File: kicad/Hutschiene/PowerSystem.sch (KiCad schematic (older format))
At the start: 16 parts, among them P201 Mode_Bridge, U201 LF120ABDT-TR, U202 TPS70933

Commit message: Further work on the redesign
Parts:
- removed D201: 12VDC, LEDs:LED_0805, symbol LED
- removed R203: 2k4Ω, Resistors_SMD:R_0805, symbol R
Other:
- moved on the sheet: TP202
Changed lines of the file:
@@
 U+
 $Comp
-L GND #PWR016
+L GND #PWR017
 U 1 1 584DB061
 P 3900 4850
-F 0 "#PWR016" H 3900 4600 50  0001 C CNN
+F 0 "#PWR017" H 3900 4600 50  0001 C CNN
 F 1 "GND" H 3900 4700 50  0000 C CNN
 F 2 "" H 3900 4850 50  0000 C CNN
@@
 $EndComp
 $Comp
-L GND #PWR017
+L GND #PWR018
 U 1 1 584DB084
 P 5250 5300
-F 0 "#PWR017" H 5250 5050 50  0001 C CNN
+F 0 "#PWR018" H 5250 5050 50  0001 C CNN
 F 1 "GND" H 5250 5150 50  0000 C CNN
 F 2 "" H 5250 5300 50  0000 C CNN
@@
 UbOut
 Wire Wire Line
-	4450 1400 6150 1400
+	4450 1400 5550 1400
 Wire Wire Line
 	2800 1400 3350 1400
@@
 $EndComp
 $Comp
-L GND #PWR018
+L GND #PWR019
 U 1 1 584DD17A
 P 3900 2650
-F 0 "#PWR018" H 3900 2400 50  0001 C CNN
+F 0 "#PWR019" H 3900 2400 50  0001 C CNN
 F 1 "GND" H 3900 2500 50  0000 C CNN
 F 2 "" H 3900 2650 50  0000 C CNN
@@
 	1    0    0    -1
 $EndComp
-Text HLabel 6150 1400 2    60   Input ~ 0
+Text HLabel 5550 1400 2    60   Input ~ 0
 U+Out
 Text HLabel 2800 1400 0    60   Input ~ 0
@@
 	4600 1700 4600 1400
 Connection ~ 4600 1400
-$Comp
-L LED D201
-U 1 1 584DD7AB
-P 5250 2300
-F 0 "D201" H 5250 2400 50  0000 C CNN
-F 1 "12VDC" H 5250 2200 50  0000 C CNN
-F 2 "LEDs:LED_0805" H 5250 2300 50  0001 C CNN
-F 3 "" H 5250 2300 50  0000 C CNN
-	1    5250 2300
-	0    -1   -1   0
-$EndComp
-Wire Wire Line
-	5250 1400 5250 1650
-Connection ~ 5250 1400
-$Comp
-L R R203
-U 1 1 584DD8C0
-P 5250 1800
-F 0 "R203" V 5330 1800 50  0000 C CNN
-F 1 "2k4Ω" V 5250 1800 50  0000 C CNN
-F 2 "Resistors_SMD:R_0805" V 5180 1800 50  0001 C CNN
-F 3 "" H 5250 1800 50  0000 C CNN
-	1    5250 1800
-	1    0    0    -1
-$EndComp
-$Comp
-L GND #PWR019
-U 1 1 584DD971
-P 5250 2650
-F 0 "#PWR019" H 5250 2400 50  0001 C CNN
-F 1 "GND" H 5250 2500 50  0000 C CNN
-F 2 "" H 5250 2650 50  0000 C CNN
-F 3 "" H 5250 2650 50  0000 C CNN
-	1    5250 2650
-	1    0    0    -1
-$EndComp
-Wire Wire Line
-	5250 2500 5250 2650
-Wire Wire Line
-	5600 1200 5600 1400
-Connection ~ 5600 1400
-Text Label 6000 1400 0    60   ~ 0
+Wire Wire Line
+	5000 1200 5000 1400
+Connection ~ 5000 1400
+Text Label 5400 1400 0    60   ~ 0
 U+
 $Comp
 L TEST_1P TP202
 U 1 1 584E1FA9
-P 5600 1200
-F 0 "TP202" H 5600 1470 50  0000 C CNN
-F 1 "TP12V" H 5600 1400 50  0000 C CNN
-F 2 "Pin_Headers:Pin_Header_Straight_1x01" H 5800 1200 50  0001 C CNN
-F 3 "" H 5800 1200 50  0000 C CNN
-F 4 "Value" H 5600 1200 60  0001 C CNN "MFP"
-F 5 "Value" H 5600 1200 60  0001 C CNN "Conrad-PN"
-F 6 "Value" H 5600 1200 60  0001 C CNN "Digikey-PN"
-	1    5600 1200
+P 5000 1200
+F 0 "TP202" H 5000 1470 50  0000 C CNN
+F 1 "TP12V" H 5000 1400 50  0000 C CNN
+F 2 "Pin_Headers:Pin_Header_Straight_1x01" H 5200 1200 50  0001 C CNN
+F 3 "" H 5200 1200 50  0000 C CNN
+F 4 "Value" H 5000 1200 60  0001 C CNN "MFP"
+F 5 "Value" H 5000 1200 60  0001 C CNN "Conrad-PN"
+F 6 "Value" H 5000 1200 60  0001 C CNN "Digikey-PN"
+	1    5000 1200
 	1    0    0    -1
 $EndComp
@@
 $EndComp
 Wire Wire Line
-	5250 2100 5250 1950
-Wire Wire Line
 	5250 4550 5250 4700

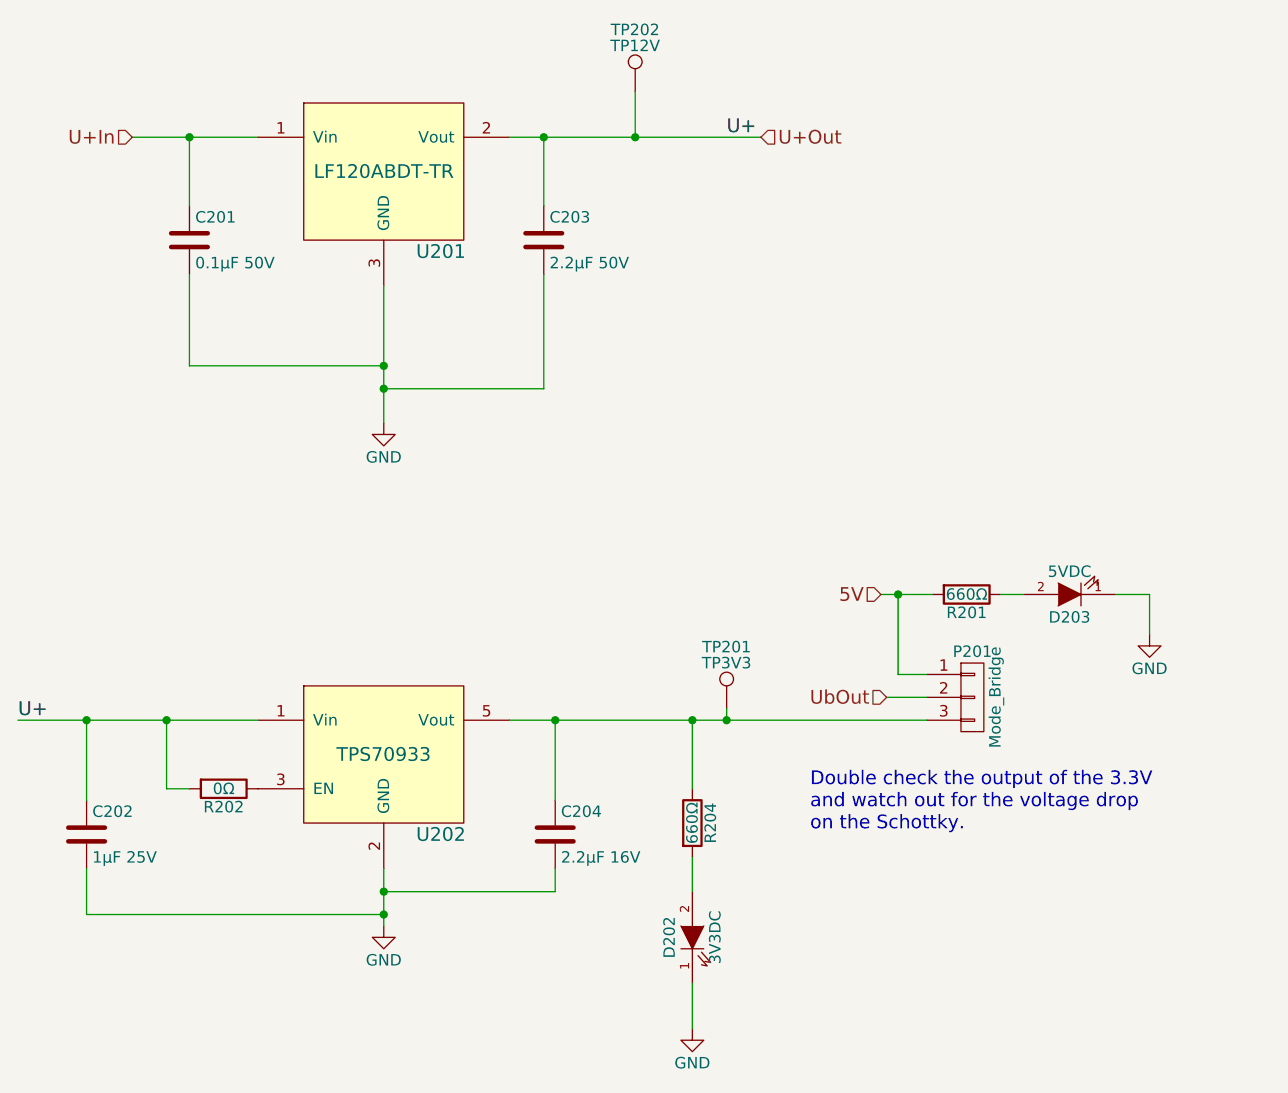
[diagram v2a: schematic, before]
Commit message: Further work on the new Hutschiene Layout
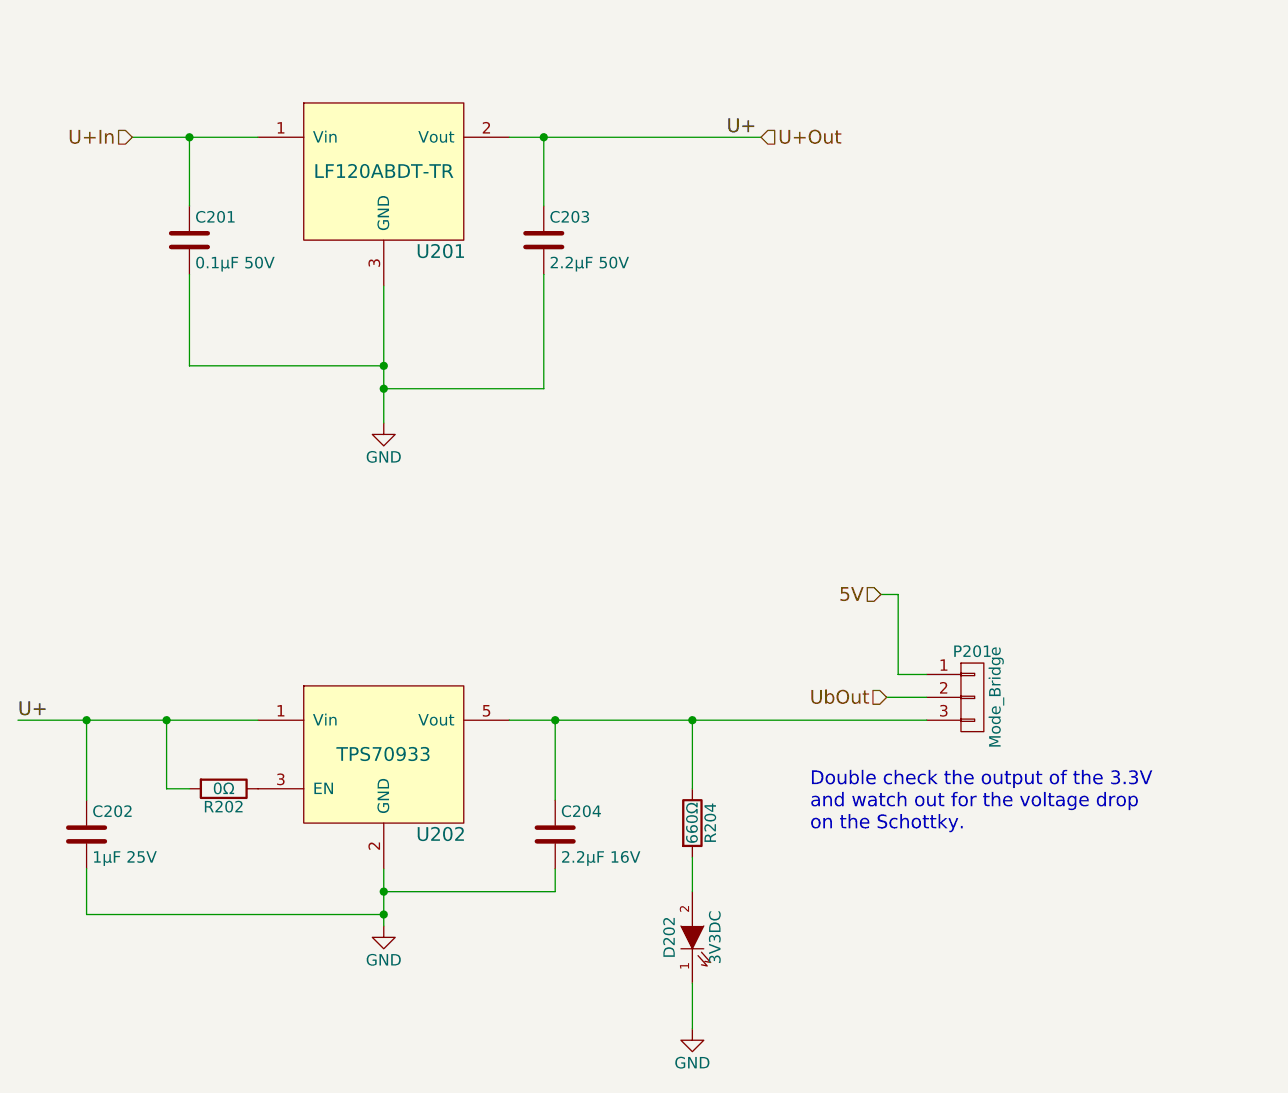
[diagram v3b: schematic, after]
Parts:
- removed D203: 5VDC, LEDs:LED_0805, symbol LED
- removed R201: 660Ω, Resistors_SMD:R_0805, symbol R
- removed TP201: TP3V3, Measurement_Points:Measurement_Point_Round-SMD-Pad_Small, symbol TEST_1P
- removed TP202: TP12V, Pin_Headers:Pin_Header_Straight_1x01, symbol TEST_1P
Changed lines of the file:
@@
 Wire Wire Line
 	5250 5100 5250 5300
-Wire Wire Line
-	5400 3950 5400 3900
-Connection ~ 5400 3950
 Text HLabel 6100 3850 0    60   Input ~ 0
 UbOut
@@
 	4600 1700 4600 1400
 Connection ~ 4600 1400
-Wire Wire Line
-	5000 1200 5000 1400
-Connection ~ 5000 1400
 Text Label 5400 1400 0    60   ~ 0
 U+
-$Comp
-L TEST_1P TP202
-U 1 1 584E1FA9
-P 5000 1200
-F 0 "TP202" H 5000 1470 50  0000 C CNN
-F 1 "TP12V" H 5000 1400 50  0000 C CNN
-F 2 "Pin_Headers:Pin_Header_Straight_1x01" H 5200 1200 50  0001 C CNN
-F 3 "" H 5200 1200 50  0000 C CNN
-F 4 "Value" H 5000 1200 60  0001 C CNN "MFP"
-F 5 "Value" H 5000 1200 60  0001 C CNN "Conrad-PN"
-F 6 "Value" H 5000 1200 60  0001 C CNN "Digikey-PN"
-	1    5000 1200
-	1    0    0    -1
-$EndComp
-$Comp
-L TEST_1P TP201
-U 1 1 584E2106
-P 5400 3900
-F 0 "TP201" H 5400 4170 50  0000 C CNN
-F 1 "TP3V3" H 5400 4100 50  0000 C CNN
-F 2 "Measurement_Points:Measurement_Point_Round-SMD-Pad_Small" H 5600 3900 50  0001 C CNN
-F 3 "" H 5600 3900 50  0000 C CNN
-	1    5400 3900
-	1    0    0    -1
-$EndComp
 Wire Wire Line
 	5250 4550 5250 4700
@@
 Wire Wire Line
 	4450 3950 6275 3950
-$Comp
-L LED D203
-U 1 1 58DCC141
-P 6900 3400
-F 0 "D203" H 6900 3500 50  0000 C CNN
-F 1 "5VDC" H 6900 3300 50  0000 C CNN
-F 2 "LEDs:LED_0805" H 6900 3400 50  0001 C CNN
-F 3 "" H 6900 3400 50  0000 C CNN
-	1    6900 3400
-	-1   0    0    1
-$EndComp
-$Comp
-L GND #PWR020
-U 1 1 58DCC147
-P 7250 3575
-F 0 "#PWR020" H 7250 3325 50  0001 C CNN
-F 1 "GND" H 7250 3425 50  0000 C CNN
-F 2 "" H 7250 3575 50  0000 C CNN
-F 3 "" H 7250 3575 50  0000 C CNN
-	1    7250 3575
-	1    0    0    -1
-$EndComp
-$Comp
-L R R201
-U 1 1 58DCC526
-P 6450 3400
-F 0 "R201" V 6530 3400 50  0000 C CNN
-F 1 "660Ω" V 6450 3400 50  0000 C CNN
-F 2 "Resistors_SMD:R_0805" V 6380 3400 50  0001 C CNN
-F 3 "" H 6450 3400 50  0000 C CNN
-	1    6450 3400
-	0    1    1    0
-$EndComp
 Wire Wire Line
-	6075 3400 6300 3400
-Wire Wire Line
-	6600 3400 6700 3400
-Wire Wire Line
-	7100 3400 7250 3400
-Wire Wire Line
-	7250 3400 7250 3575
+	6075 3400 6150 3400
 Wire Wire Line
 	6275 3750 6150 3750
 Wire Wire Line
 	6150 3750 6150 3400
-Connection ~ 6150 3400
 $EndSCHEMATC

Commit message: Correction to the board connected and seperated out the pwr
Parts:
- C204: footprint Capacitors_SMD:C_1210 -> Capacitors_SMD:C_1206
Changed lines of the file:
@@
 U+
 $Comp
-L GND #PWR017
+L GND #PWR019
 U 1 1 584DB061
 P 3900 4850
-F 0 "#PWR017" H 3900 4600 50  0001 C CNN
+F 0 "#PWR019" H 3900 4600 50  0001 C CNN
 F 1 "GND" H 3900 4700 50  0000 C CNN
 F 2 "" H 3900 4850 50  0000 C CNN
@@
 F 0 "C204" H 4675 4550 50  0000 L CNN
 F 1 "2.2μF 16V" H 4675 4350 50  0000 L CNN
-F 2 "Capacitors_SMD:C_1210" H 4688 4300 50  0001 C CNN
+F 2 "Capacitors_SMD:C_1206" H 4688 4300 50  0001 C CNN
 F 3 "" H 4650 4450 50  0000 C CNN
 F 4 "Value" H 4650 4450 60  0001 C CNN "MFP"
@@
 $EndComp
 $Comp
-L GND #PWR018
+L GND #PWR020
 U 1 1 584DB084
 P 5250 5300
-F 0 "#PWR018" H 5250 5050 50  0001 C CNN
+F 0 "#PWR020" H 5250 5050 50  0001 C CNN
 F 1 "GND" H 5250 5150 50  0000 C CNN
 F 2 "" H 5250 5300 50  0000 C CNN
@@
 $EndComp
 $Comp
-L GND #PWR019
+L GND #PWR021
 U 1 1 584DD17A
 P 3900 2650
-F 0 "#PWR019" H 3900 2400 50  0001 C CNN
+F 0 "#PWR021" H 3900 2400 50  0001 C CNN
 F 1 "GND" H 3900 2500 50  0000 C CNN
 F 2 "" H 3900 2650 50  0000 C CNN

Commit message: More refinements based on the DIN prototype tests
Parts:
- C201: footprint Capacitors_SMD:C_0805 -> Capacitors_SMD:C_0805_HandSoldering
- C202: footprint Capacitors_SMD:C_1210 -> Capacitors_SMD:C_1210_HandSoldering
- C203, C204: footprint Capacitors_SMD:C_1206 -> Capacitors_SMD:C_1206_HandSoldering
- D202: footprint LEDs:LED_0805 -> LEDs:LED_0805_HandSoldering
- R202, R204: footprint Resistors_SMD:R_0805 -> Resistors_SMD:R_0805_HandSoldering
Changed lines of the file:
@@
 F 0 "R202" V 3280 4250 50  0000 C CNN
 F 1 "0Ω" V 3200 4250 50  0000 C CNN
-F 2 "Resistors_SMD:R_0805" V 3130 4250 50  0001 C CNN
+F 2 "Resistors_SMD:R_0805_HandSoldering" V 3130 4250 50  0001 C CNN
 F 3 "" H 3200 4250 50  0000 C CNN
 	1    3200 4250
@@
 F 0 "C202" H 2625 4550 50  0000 L CNN
 F 1 "1μF 25V" H 2625 4350 50  0000 L CNN
-F 2 "Capacitors_SMD:C_1210" H 2638 4300 50  0001 C CNN
+F 2 "Capacitors_SMD:C_1210_HandSoldering" H 2638 4300 50  0001 C CNN
 F 3 "" H 2600 4450 50  0000 C CNN
 F 4 "Value" H 2600 4450 60  0001 C CNN "MFP"
@@
 F 0 "C204" H 4675 4550 50  0000 L CNN
 F 1 "2.2μF 16V" H 4675 4350 50  0000 L CNN
-F 2 "Capacitors_SMD:C_1206" H 4688 4300 50  0001 C CNN
+F 2 "Capacitors_SMD:C_1206_HandSoldering" H 4688 4300 50  0001 C CNN
 F 3 "" H 4650 4450 50  0000 C CNN
 F 4 "Value" H 4650 4450 60  0001 C CNN "MFP"
@@
 F 0 "D202" H 5250 5000 50  0000 C CNN
 F 1 "3V3DC" H 5250 4800 50  0000 C CNN
-F 2 "LEDs:LED_0805" H 5250 4900 50  0001 C CNN
+F 2 "LEDs:LED_0805_HandSoldering" H 5250 4900 50  0001 C CNN
 F 3 "" H 5250 4900 50  0000 C CNN
 	1    5250 4900
@@
 F 0 "R204" V 5330 4400 50  0000 C CNN
 F 1 "660Ω" V 5250 4400 50  0000 C CNN
-F 2 "Resistors_SMD:R_0805" V 5180 4400 50  0001 C CNN
+F 2 "Resistors_SMD:R_0805_HandSoldering" V 5180 4400 50  0001 C CNN
 F 3 "" H 5250 4400 50  0000 C CNN
 	1    5250 4400
@@
 F 0 "C201" H 3075 1950 50  0000 L CNN
 F 1 "0.1μF 50V" H 3075 1750 50  0000 L CNN
-F 2 "Capacitors_SMD:C_0805" H 3088 1700 50  0001 C CNN
+F 2 "Capacitors_SMD:C_0805_HandSoldering" H 3088 1700 50  0001 C CNN
 F 3 "" H 3050 1850 50  0000 C CNN
 	1    3050 1850
@@
 F 0 "C203" H 4625 1950 50  0000 L CNN
 F 1 "2.2μF 50V" H 4625 1750 50  0000 L CNN
-F 2 "Capacitors_SMD:C_1206" H 4638 1700 50  0001 C CNN
+F 2 "Capacitors_SMD:C_1206_HandSoldering" H 4638 1700 50  0001 C CNN
 F 3 "" H 4600 1850 50  0000 C CNN
 F 4 "CL32B225KBJNNNE" H 4600 1850 60  0001 C CNN "MFP"

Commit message: In preperation for using a stencil - moved most 0805 back from handsolder to normal
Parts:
- C201: footprint Capacitors_SMD:C_0805_HandSoldering -> Capacitors_SMD:C_0805
- C202: footprint Capacitors_SMD:C_1210_HandSoldering -> Capacitors_SMD:C_0805
- C203, C204: footprint Capacitors_SMD:C_1206_HandSoldering -> Capacitors_SMD:C_0805
- R202: footprint Resistors_SMD:R_0805_HandSoldering -> Resistors_SMD:R_0805
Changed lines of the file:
@@
 F 0 "R202" V 3280 4250 50  0000 C CNN
 F 1 "0Ω" V 3200 4250 50  0000 C CNN
-F 2 "Resistors_SMD:R_0805_HandSoldering" V 3130 4250 50  0001 C CNN
+F 2 "Resistors_SMD:R_0805" V 3130 4250 50  0001 C CNN
 F 3 "" H 3200 4250 50  0000 C CNN
 	1    3200 4250
@@
 F 0 "C202" H 2625 4550 50  0000 L CNN
 F 1 "1μF 25V" H 2625 4350 50  0000 L CNN
-F 2 "Capacitors_SMD:C_1210_HandSoldering" H 2638 4300 50  0001 C CNN
+F 2 "Capacitors_SMD:C_0805" H 2638 4300 50  0001 C CNN
 F 3 "" H 2600 4450 50  0000 C CNN
 F 4 "Value" H 2600 4450 60  0001 C CNN "MFP"
@@
 F 0 "C204" H 4675 4550 50  0000 L CNN
 F 1 "2.2μF 16V" H 4675 4350 50  0000 L CNN
-F 2 "Capacitors_SMD:C_1206_HandSoldering" H 4688 4300 50  0001 C CNN
+F 2 "Capacitors_SMD:C_0805" H 4688 4300 50  0001 C CNN
 F 3 "" H 4650 4450 50  0000 C CNN
 F 4 "Value" H 4650 4450 60  0001 C CNN "MFP"
@@
 F 0 "C201" H 3075 1950 50  0000 L CNN
 F 1 "0.1μF 50V" H 3075 1750 50  0000 L CNN
-F 2 "Capacitors_SMD:C_0805_HandSoldering" H 3088 1700 50  0001 C CNN
+F 2 "Capacitors_SMD:C_0805" H 3088 1700 50  0001 C CNN
 F 3 "" H 3050 1850 50  0000 C CNN
 	1    3050 1850
@@
 F 0 "C203" H 4625 1950 50  0000 L CNN
 F 1 "2.2μF 50V" H 4625 1750 50  0000 L CNN
-F 2 "Capacitors_SMD:C_1206_HandSoldering" H 4638 1700 50  0001 C CNN
+F 2 "Capacitors_SMD:C_0805" H 4638 1700 50  0001 C CNN
 F 3 "" H 4600 1850 50  0000 C CNN
 F 4 "CL32B225KBJNNNE" H 4600 1850 60  0001 C CNN "MFP"

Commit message: Moved the RJ45 for the back-plane placement
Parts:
- D202: symbol LED -> LED-RESCUE-tl2c
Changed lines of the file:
@@
 EESchema Schematic File Version 2
+LIBS:tl2c-rescue
 LIBS:tl2c-symbols
 LIBS:power
@@
 $EndComp
 $Comp
-L LED D202
+L LED-RESCUE-tl2c D202
 U 1 1 584DB076
 P 5250 4900
+AR Path="/584DB076" Ref="D202"  Part="1"
+AR Path="/584D9013/584DB076" Ref="D202"  Part="1"
 F 0 "D202" H 5250 5000 50  0000 C CNN
 F 1 "3V3DC" H 5250 4800 50  0000 C CNN

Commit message: Upgrade to KiCad 5.1
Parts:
- C201, C202, C203, C204: symbol C -> Device:C
- D202: symbol LED-RESCUE-tl2c -> tl2c-rescue:LED-RESCUE-tl2c
- P201: symbol CONN_01X03 -> tl2c-rescue:CONN_01X03
- R202, R204: symbol R -> Device:R
- U201: symbol LF120ABDT-TR -> tl2c-symbols:LF120ABDT-TR
- U202: symbol TPS70933 -> tl2c-symbols:TPS70933
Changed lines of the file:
@@
-EESchema Schematic File Version 2
-LIBS:tl2c-rescue
-LIBS:tl2c-symbols
-LIBS:power
-LIBS:device
-LIBS:transistors
-LIBS:conn
-LIBS:linear
-LIBS:regul
-LIBS:74xx
-LIBS:cmos4000
-LIBS:adc-dac
-LIBS:memory
-LIBS:xilinx
-LIBS:microcontrollers
-LIBS:dsp
-LIBS:microchip
-LIBS:analog_switches
-LIBS:motorola
-LIBS:texas
-LIBS:intel
-LIBS:audio
-LIBS:interface
-LIBS:digital-audio
-LIBS:philips
-LIBS:display
-LIBS:cypress
-LIBS:siliconi
-LIBS:opto
-LIBS:atmel
-LIBS:contrib
-LIBS:valves
+EESchema Schematic File Version 4
 LIBS:tl2c-cache
-EELAYER 25 0
+EELAYER 26 0
 EELAYER END
 $Descr A4 11693 8268
@@
 $EndDescr
 $Comp
-L R R202
+L Device:R R202
 U 1 1 584DB059
 P 3200 4250
@@
 U+
 $Comp
-L GND #PWR019
+L power:GND #PWR019
 U 1 1 584DB061
 P 3900 4850
@@
 $EndComp
 $Comp
-L C C202
+L Device:C C202
 U 1 1 584DB067
 P 2600 4450
@@
 $EndComp
 $Comp
-L C C204
+L Device:C C204
 U 1 1 584DB06E
 P 4650 4450
@@
 $EndComp
 $Comp
-L LED-RESCUE-tl2c D202
+L tl2c-rescue:LED-RESCUE-tl2c D202
 U 1 1 584DB076
 P 5250 4900
@@
 $EndComp
 $Comp
-L R R204
+L Device:R R204
 U 1 1 584DB07D
 P 5250 4400
@@
 $EndComp
 $Comp
-L GND #PWR020
+L power:GND #PWR020
 U 1 1 584DB084
 P 5250 5300
@@
 $EndComp
 $Comp
-L TPS70933 U202
+L tl2c-symbols:TPS70933 U202
 U 1 1 584DB0C1
 P 3900 4100
@@
 $EndComp
 $Comp
-L LF120ABDT-TR U201
+L tl2c-symbols:LF120ABDT-TR U201
 U 1 1 584DB84E
 P 3900 1550
@@
 	2800 1400 3350 1400
 $Comp
-L C C201
+L Device:C C201
 U 1 1 584DCFF9
 P 3050 1850
@@
 $EndComp
 $Comp
-L C C203
+L Device:C C203
 U 1 1 584DD0BF
 P 4600 1850
@@
 $EndComp
 $Comp
-L GND #PWR021
+L power:GND #PWR021
 U 1 1 584DD17A
 P 3900 2650
@@
 Double check the output of the 3.3V\nand watch out for the voltage drop \non the Schottky.
 $Comp
-L CONN_01X03 P201
+L tl2c-rescue:CONN_01X03 P201
 U 1 1 58DCB84B
 P 6475 3850
